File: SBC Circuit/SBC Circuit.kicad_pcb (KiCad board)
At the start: 2 copper layers, 127 x 114.3 mm, 91 parts, among them J1 USB_B, J2 Conn_01x02_Pin, J3 Conn_01x06_Pin, J4 Conn_01x06_Pin, J5 Conn_01x03_Pin, J6 Conn_01x08_Pin, J7 Conn_01x06_Pin, J8 Conn_01x02_Pin, J9 Conn_02x04_Odd_Even, Q1 AOI21357, Q2 AOI21357, SW1 RESET, U1 MC68000FN, U10 FT230XS, U11 MC34064P, U2 XC9572XL, U3 68681, U4 MCM6206CP, U5 MCM6206CP, U6 28C256, U7 28C256, U8 LM7805_TO220, U9 LD1117AV33, X1 SG-531, X2 EC11

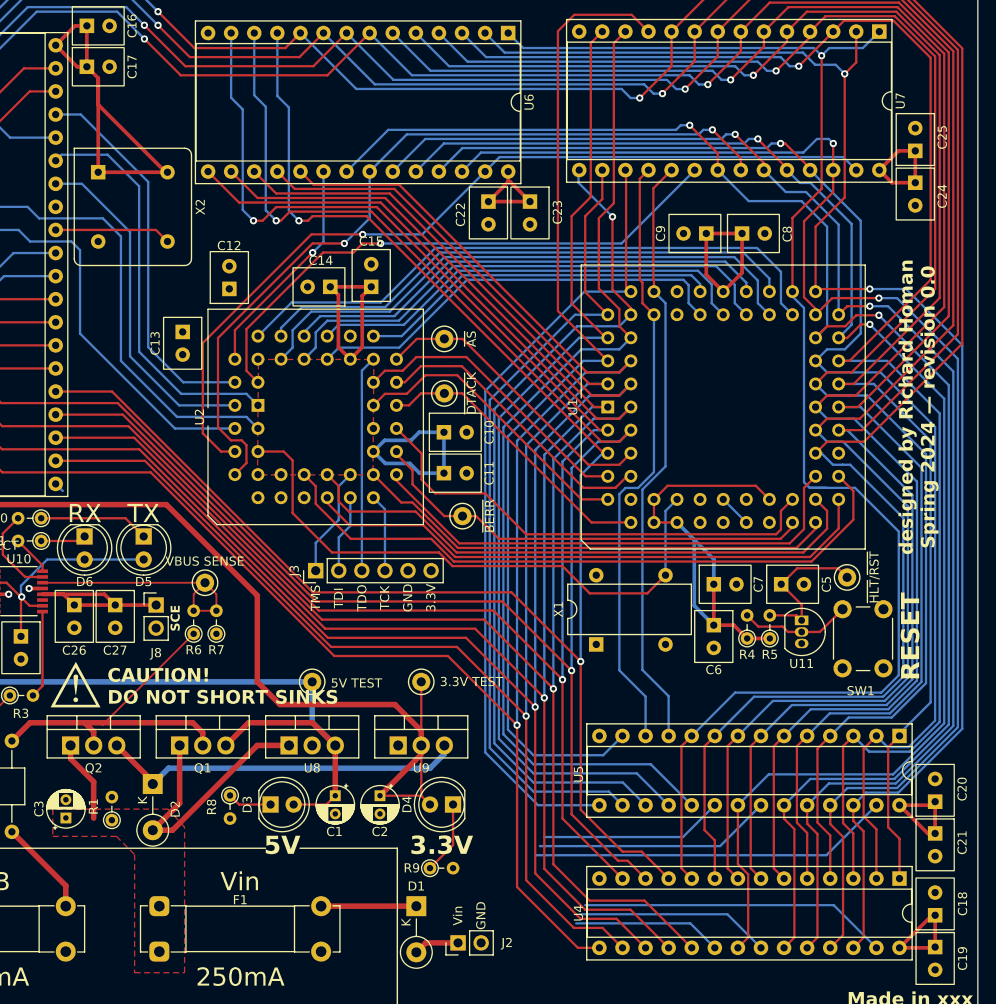
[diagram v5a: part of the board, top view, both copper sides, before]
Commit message: Connect some power lines
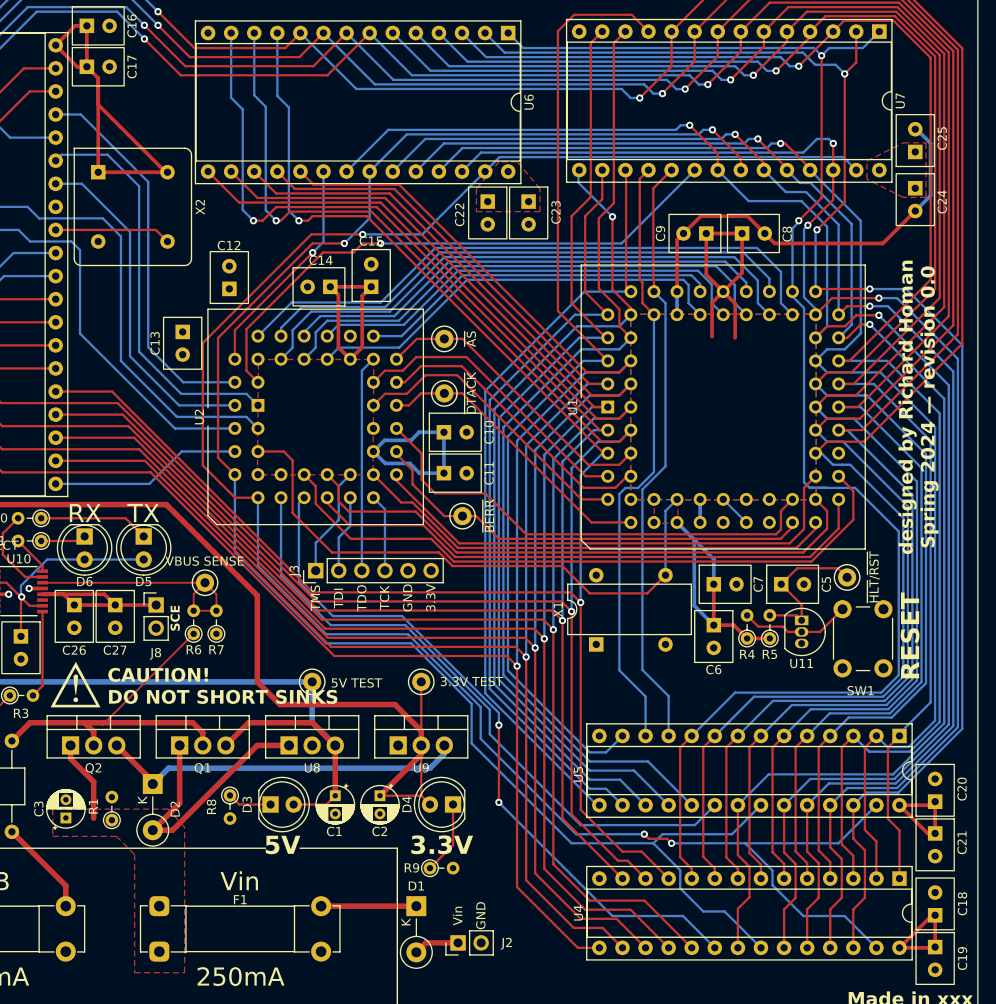
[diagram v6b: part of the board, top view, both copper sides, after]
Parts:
- moved C24 0.62 mm to (196.3, 55.4)
- moved C23 0.15 mm to (153.8, 56.9)
- moved C25 0.12 mm to (196.3, 51.4)
- moved C22 0.08 mm to (149.3, 56.9)
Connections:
- U2 pad 11: ramh_cs -> raml_cs
- U2 pad 4: we -> duart_irq
- U2 pad 7: duart_irq -> we
- U2 pad 9: raml_cs -> ramh_cs
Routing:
- net raml_cs: track 16.4 -> 77.7 mm, vias 0 -> 2
- net oe: track 137.7 -> 190.2 mm
- net GNDREF: track 2.61 -> 53.9 mm
- net ramh_cs: track 20.2 -> 70.2 mm
- net we: track 169.1 -> 214.1 mm, vias 1 -> 3
- net +5V: track 283.1 -> 250.2 mm
- net duart_irq: track 1.10 -> 21.2 mm
- net data8: track 111.4 -> 107.3 mm
- net data13: track 88.9 -> 85.1 mm
- net data11: track 93.9 -> 90.1 mm
- net data9: track 112.2 -> 108.4 mm
- net data12: track 90.1 -> 86.3 mm
- net data10: track 109.5 -> 105.7 mm
- net data7: track 201.2 -> 198.5 mm
- net data6: track 182.7 -> 180.0 mm
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- added copper zone on F.Cu, net +5V
- added copper zone on B.Cu, net GNDREF

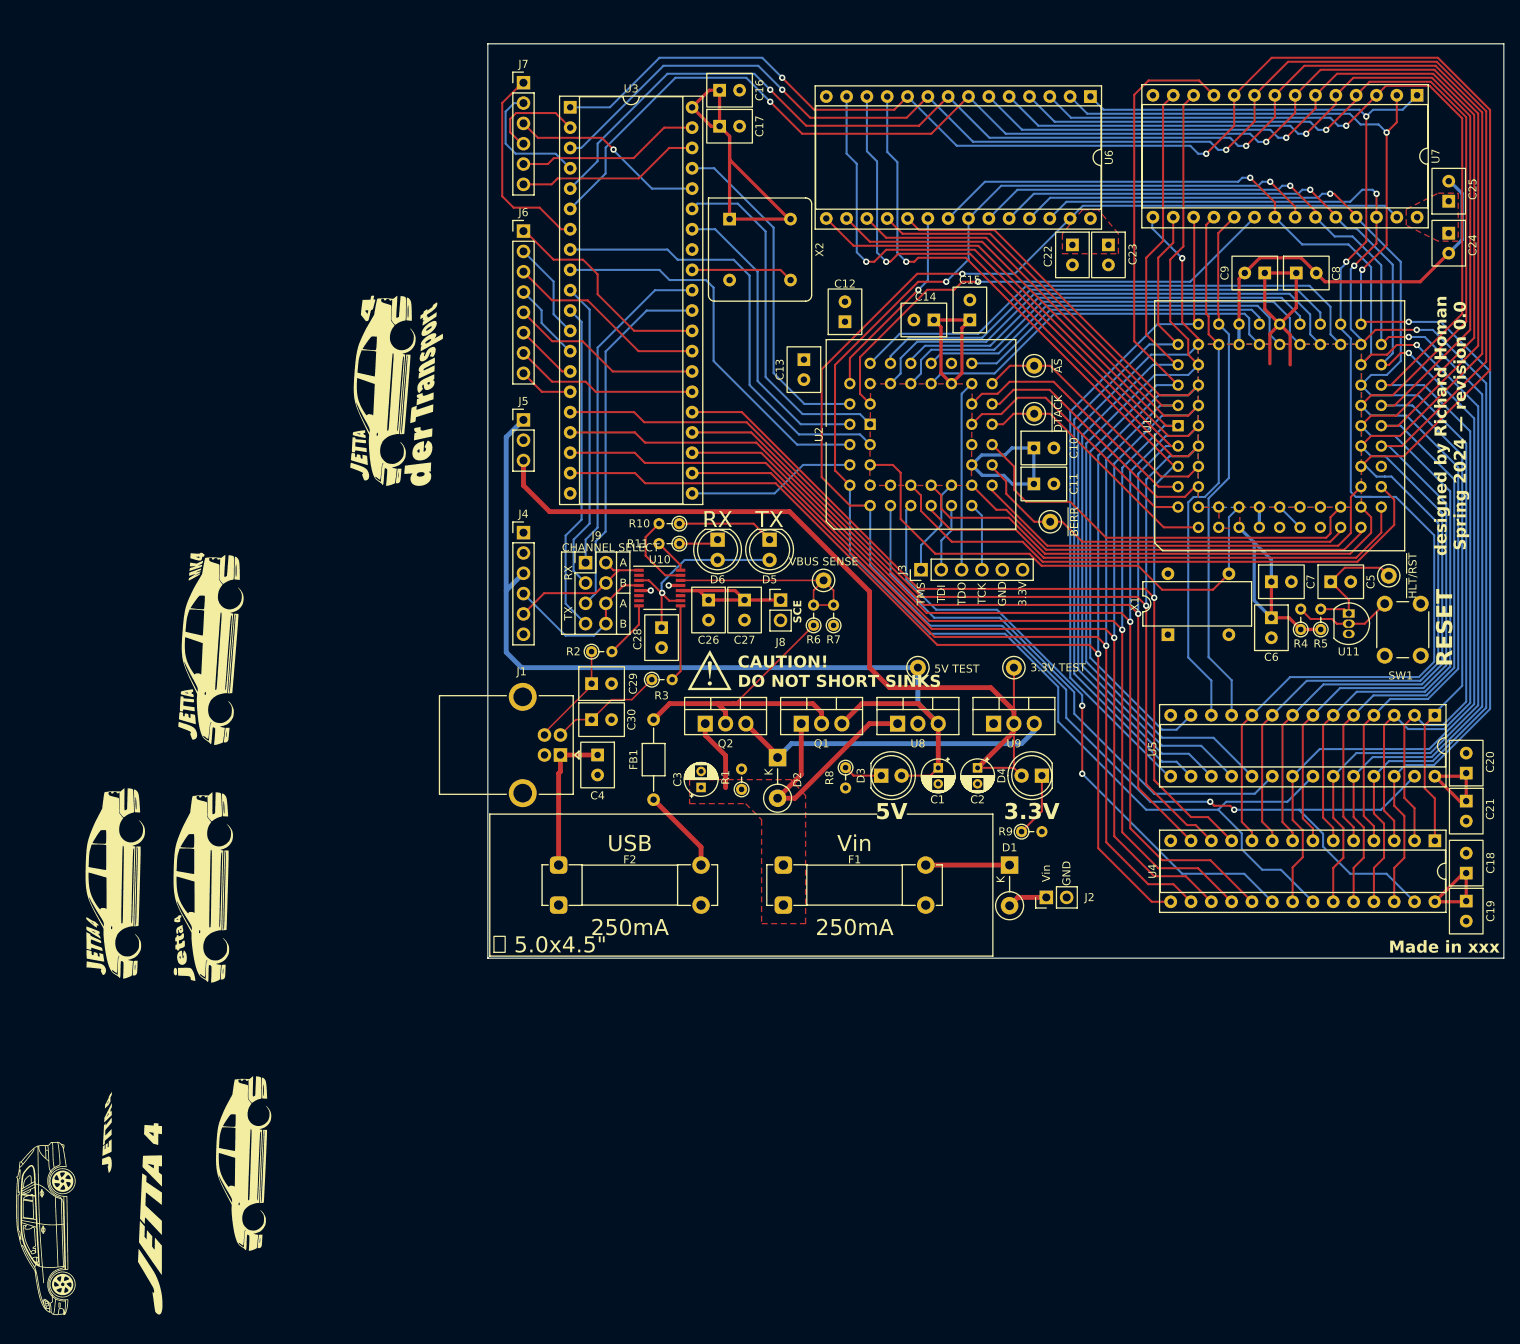
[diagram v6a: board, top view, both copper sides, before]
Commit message: All lines connected
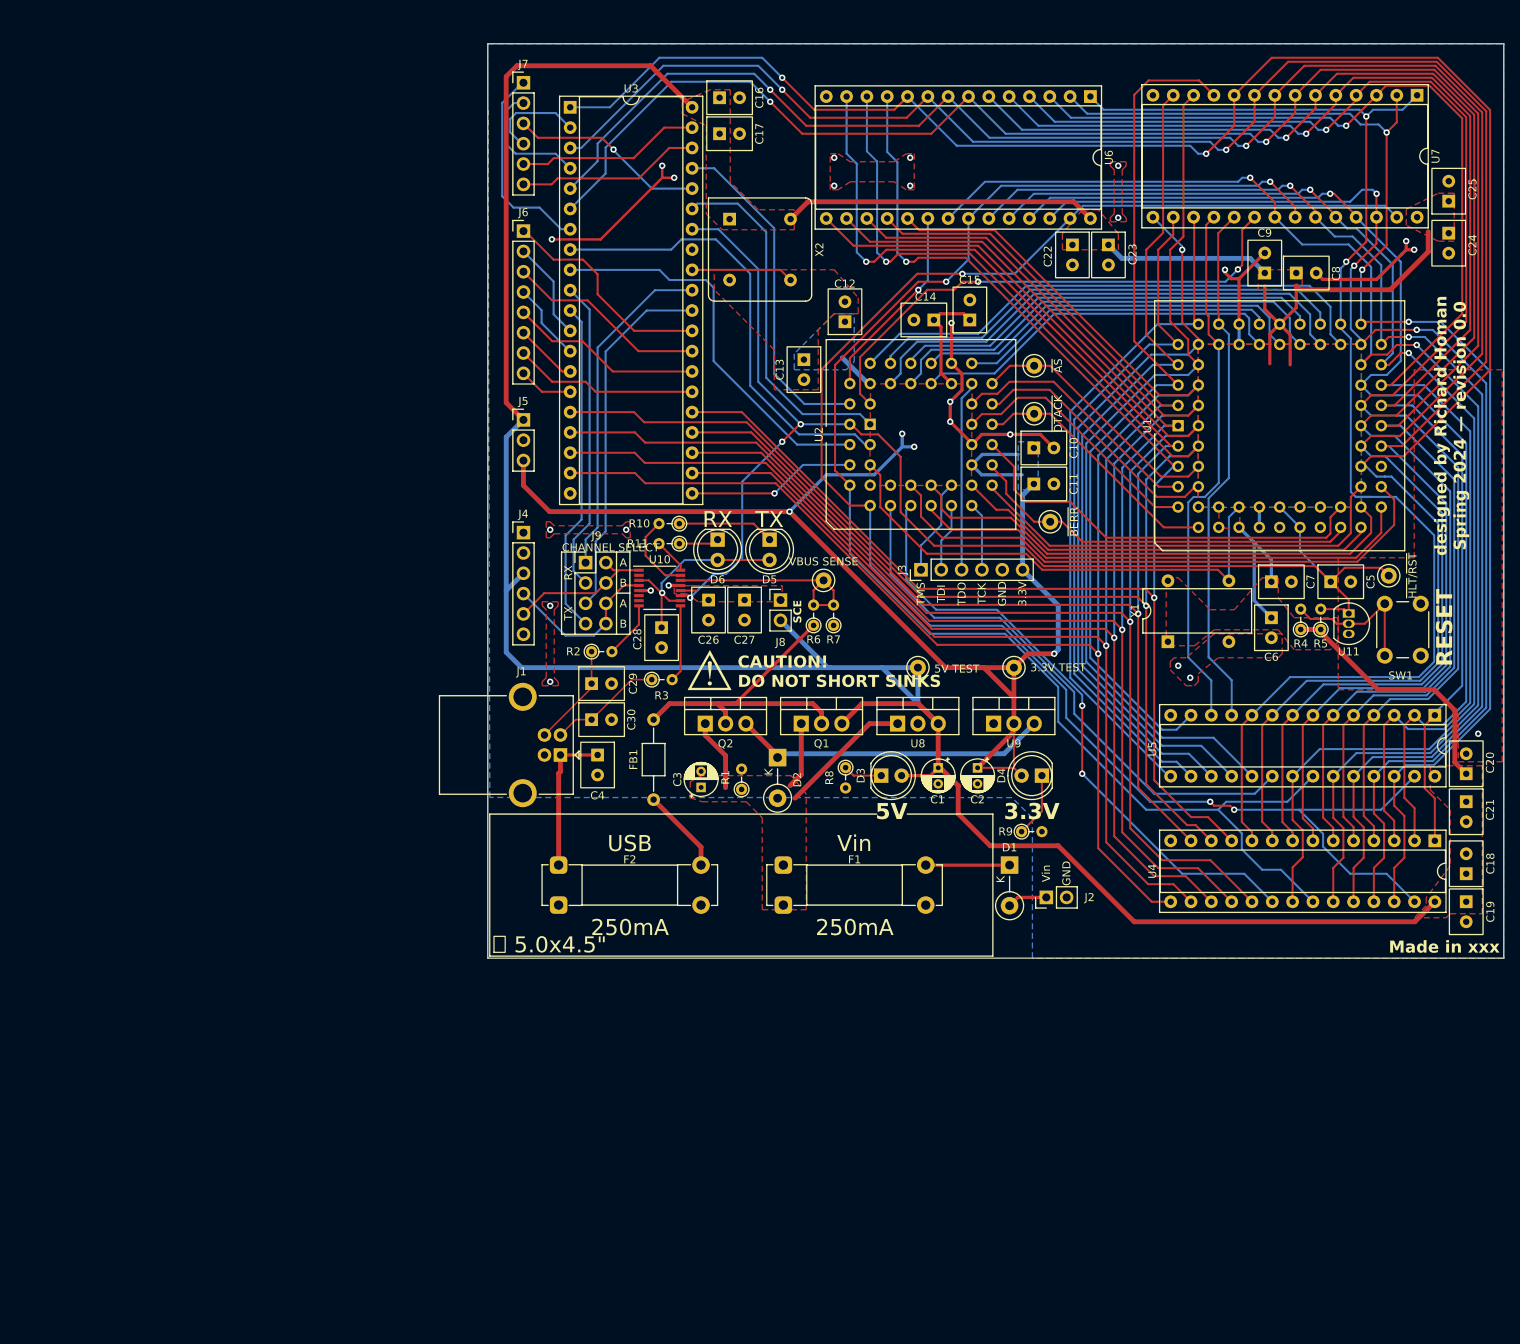
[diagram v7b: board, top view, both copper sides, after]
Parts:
- removed G*** (x9): LOGO, LOGO
- moved C16 0.94 mm to (105.2, 38.5)
- moved C17 0.94 mm to (105.2, 43.0)
- moved X1 0.88 mm to (161.2, 106.5)
- moved C18 0.08 mm to (198.5, 135.5)
- moved C19 0.08 mm to (198.5, 139.0)
- moved C20 0.08 mm to (198.5, 123.0)
- moved C21 0.08 mm to (198.5, 126.5)
- turned C9 to 90 degrees
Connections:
- net Net-(U10-USBDM) renamed /Power+IO/n10
- net Net-(U10-USBDP) renamed /Power+IO/n9
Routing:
- net +5V: track 250.2 -> 432.2 mm
- net hlt_rst: track 58.4 -> 169.1 mm, vias 0 -> 3
- net +3.3V: track 153.6 -> 188.3 mm, vias 0 -> 4
- net GNDREF: track 53.9 -> 84.7 mm, vias 2 -> 25
- net /Power+IO/n7: track 21.5 -> 2.11 mm
- net /n6: track 12.3 -> 18.8 mm
- net /Power+IO/vin: track 38.5 -> 34.1 mm
- net romh_cs: track 63.0 -> 65.5 mm, vias 1 -> 2
- net clk: track 64.9 -> 62.9 mm
- net duart_rw: track 55.6 -> 56.8 mm
- net /Power+IO/n5: track 40.3 -> 39.7 mm
- net duart_irq: vias 0 -> 1
- added copper zone on B.Cu, net +3.3V
- added copper zone on F.Cu, net /Power+IO/n7
- added copper zone on F.Cu, net GNDREF
